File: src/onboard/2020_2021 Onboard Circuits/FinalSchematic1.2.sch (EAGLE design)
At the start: 79 parts, among them IC1 MIC2937A-5.0BT, IC3 A5975D

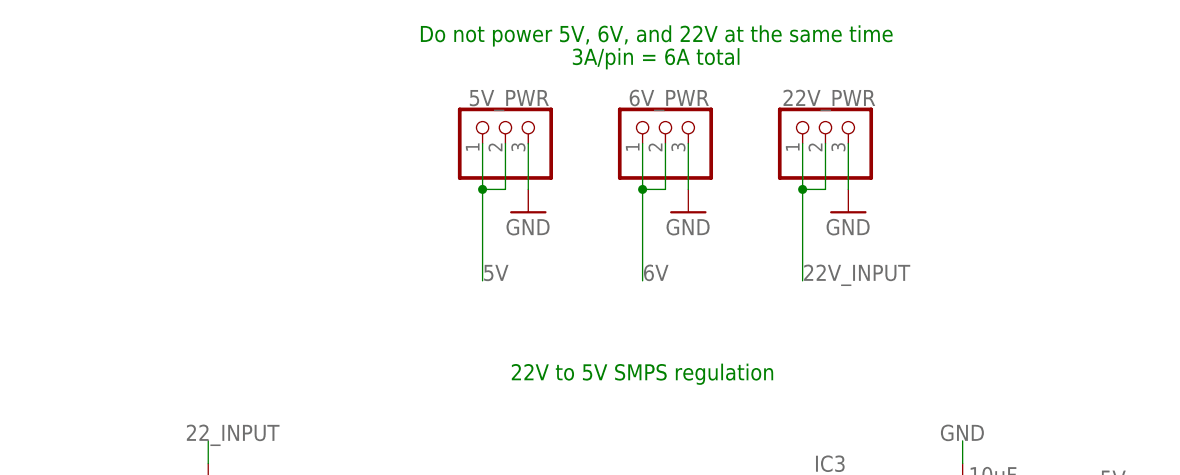
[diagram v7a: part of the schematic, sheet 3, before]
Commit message: Added bulk decoupling
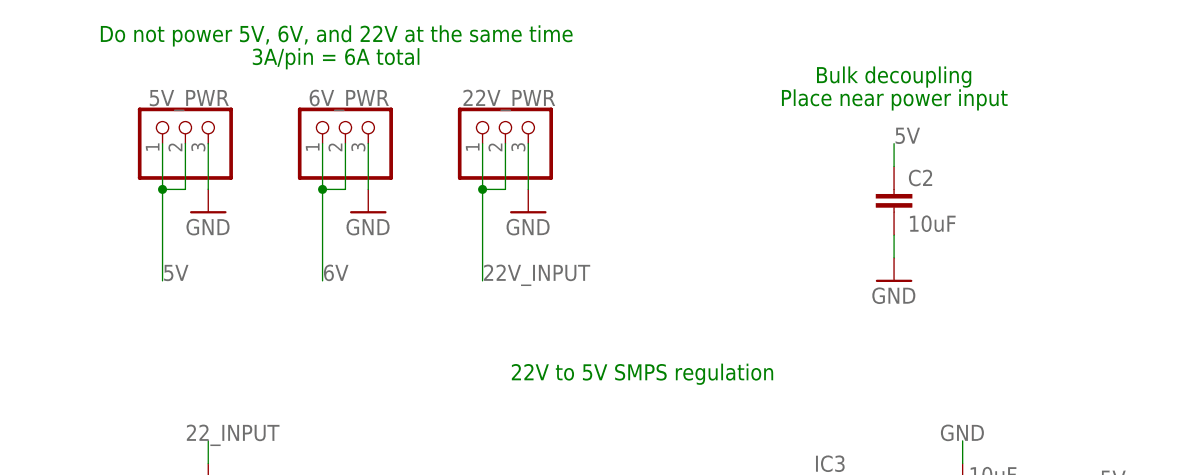
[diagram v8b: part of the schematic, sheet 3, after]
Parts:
- added C2: 10uF, capacitor-wima:C2,5-3
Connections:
- net 5V: now also C2.1
- net GND: now also C2.2
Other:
- note added: "Bulk decoupling"
- note added: "Place near power input"
- moved on the sheet: 22V_PWR, 5V_PWR, 6V_PWR
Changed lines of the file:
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@@
 <part name="GND12" library="supply1" library_urn="urn:adsk.eagle:library:371" deviceset="GND" device=""/>
 <part name="GND15" library="supply1" library_urn="urn:adsk.eagle:library:371" deviceset="GND" device=""/>
+<part name="C2" library="capacitor-wima" library_urn="urn:adsk.eagle:library:116" deviceset="C" device="2,5-3" package3d_urn="urn:adsk.eagle:package:5436/1" value="10uF"/>
+<part name="GND16" library="supply1" library_urn="urn:adsk.eagle:library:371" deviceset="GND" device=""/>
 </parts>
 <sheets>
@@
 <description>Voltage regulation</description>
 <plain>
-<text x="26.924" y="88.392" size="1.778" layer="91" align="center">Do not power 5V, 6V, and 22V at the same time</text>
-<text x="26.924" y="85.852" size="1.778" layer="91" align="center">3A/pin = 6A total</text>
+<text x="-8.636" y="88.392" size="1.778" layer="91" align="center">Do not power 5V, 6V, and 22V at the same time</text>
+<text x="-8.636" y="85.852" size="1.778" layer="91" align="center">3A/pin = 6A total</text>
 <text x="25.4" y="50.8" size="1.778" layer="91" align="center">22V to 5V SMPS regulation</text>
 <text x="22.86" y="-5.08" size="1.778" layer="91" align="center">6V to 5V LDO regulation</text>
+<text x="53.34" y="83.82" size="1.778" layer="91" align="center">Bulk decoupling</text>
+<text x="53.34" y="81.28" size="1.778" layer="91" align="center">Place near power input</text>
 </plain>
 <instances>
@@
 <attribute name="VALUE" x="67.056" y="40.259" size="1.778" layer="96" rot="R180"/>
 </instance>
-<instance part="GND11" gate="1" x="30.48" y="68.58" smashed="yes">
-<attribute name="VALUE" x="27.94" y="66.04" size="1.778" layer="96"/>
-</instance>
-<instance part="6V_PWR" gate="A" x="27.94" y="78.74" smashed="yes" rot="R90">
-<attribute name="NAME" x="28.321" y="81.28" size="1.778" layer="95" align="center"/>
-<attribute name="VALUE" x="35.56" y="72.39" size="1.778" layer="96" rot="R90"/>
-</instance>
-<instance part="22V_PWR" gate="A" x="45.72" y="78.74" smashed="yes" rot="R90">
-<attribute name="NAME" x="46.101" y="81.28" size="1.778" layer="95" align="center"/>
-<attribute name="VALUE" x="53.34" y="72.39" size="1.778" layer="96" rot="R90"/>
-</instance>
-<instance part="GND14" gate="1" x="48.26" y="68.58" smashed="yes">
-<attribute name="VALUE" x="45.72" y="66.04" size="1.778" layer="96"/>
+<instance part="GND11" gate="1" x="-5.08" y="68.58" smashed="yes">
+<attribute name="VALUE" x="-7.62" y="66.04" size="1.778" layer="96"/>
+</instance>
+<instance part="6V_PWR" gate="A" x="-7.62" y="78.74" smashed="yes" rot="R90">
+<attribute name="NAME" x="-7.239" y="81.28" size="1.778" layer="95" align="center"/>
+<attribute name="VALUE" x="0" y="72.39" size="1.778" layer="96" rot="R90"/>
+</instance>
+<instance part="22V_PWR" gate="A" x="10.16" y="78.74" smashed="yes" rot="R90">
+<attribute name="NAME" x="10.541" y="81.28" size="1.778" layer="95" align="center"/>
+<attribute name="VALUE" x="17.78" y="72.39" size="1.778" layer="96" rot="R90"/>
+</instance>
+<instance part="GND14" gate="1" x="12.7" y="68.58" smashed="yes">
+<attribute name="VALUE" x="10.16" y="66.04" size="1.778" layer="96"/>
 </instance>
 <instance part="R1" gate="G$1" x="-22.86" y="35.56" smashed="yes" rot="R90">
@@
 <attribute name="VALUE" x="-25.4" y="7.62" size="1.778" layer="96"/>
 </instance>
-<instance part="GND7" gate="1" x="12.7" y="68.58" smashed="yes">
-<attribute name="VALUE" x="10.16" y="66.04" size="1.778" layer="96"/>
-</instance>
-<instance part="5V_PWR" gate="A" x="10.16" y="78.74" smashed="yes" rot="R90">
-<attribute name="NAME" x="10.541" y="81.28" size="1.778" layer="95" align="center"/>
-<attribute name="VALUE" x="17.78" y="72.39" size="1.778" layer="96" rot="R90"/>
+<instance part="GND7" gate="1" x="-22.86" y="68.58" smashed="yes">
+<attribute name="VALUE" x="-25.4" y="66.04" size="1.778" layer="96"/>
+</instance>
+<instance part="5V_PWR" gate="A" x="-25.4" y="78.74" smashed="yes" rot="R90">
+<attribute name="NAME" x="-25.019" y="81.28" size="1.778" layer="95" align="center"/>
+<attribute name="VALUE" x="-17.78" y="72.39" size="1.778" layer="96" rot="R90"/>
 </instance>
 <instance part="IC1" gate="A1" x="20.32" y="-20.32" smashed="yes">
@@
 <attribute name="NAME" x="37.084" y="-22.479" size="1.778" layer="95"/>
 <attribute name="VALUE" x="37.084" y="-27.559" size="1.778" layer="96"/>
+</instance>
+<instance part="C2" gate="G$1" x="53.34" y="71.12" smashed="yes">
+<attribute name="NAME" x="54.864" y="71.501" size="1.778" layer="95"/>
+<attribute name="VALUE" x="54.864" y="66.421" size="1.778" layer="96"/>
+</instance>
+<instance part="GND16" gate="1" x="53.34" y="60.96" smashed="yes">
+<attribute name="VALUE" x="50.8" y="58.42" size="1.778" layer="96"/>
 </instance>
 </instances>
@@
 </segment>
 <segment>
-<wire x1="7.62" y1="76.2" x2="7.62" y2="71.12" width="0.1524" layer="91"/>
-<label x="7.62" y="60.96" size="1.778" layer="95"/>
+<wire x1="-27.94" y1="76.2" x2="-27.94" y2="71.12" width="0.1524" layer="91"/>
+<label x="-27.94" y="60.96" size="1.778" layer="95"/>
 <pinref part="5V_PWR" gate="A" pin="1"/>
 <pinref part="5V_PWR" gate="A" pin="2"/>
-<wire x1="7.62" y1="71.12" x2="7.62" y2="60.96" width="0.1524" layer="91"/>
-<wire x1="10.16" y1="76.2" x2="10.16" y2="71.12" width="0.1524" layer="91"/>
-<wire x1="10.16" y1="71.12" x2="7.62" y2="71.12" width="0.1524" layer="91"/>
-<junction x="7.62" y="71.12"/>
+<wire x1="-27.94" y1="71.12" x2="-27.94" y2="60.96" width="0.1524" layer="91"/>
+<wire x1="-25.4" y1="76.2" x2="-25.4" y2="71.12" width="0.1524" layer="91"/>
+<wire x1="-25.4" y1="71.12" x2="-27.94" y2="71.12" width="0.1524" layer="91"/>
+<junction x="-27.94" y="71.12"/>
 </segment>
 <segment>
@@
 <label x="48.26" y="-20.32" size="1.778" layer="95"/>
 </segment>
+<segment>
+<pinref part="C2" gate="G$1" pin="1"/>
+<wire x1="53.34" y1="73.66" x2="53.34" y2="76.2" width="0.1524" layer="91"/>
+<label x="53.34" y="76.2" size="1.778" layer="95"/>
+</segment>
 </net>
 <net name="3.3V" class="0">
@@
 </segment>
 <segment>
-<wire x1="30.48" y1="76.2" x2="30.48" y2="71.12" width="0.1524" layer="91"/>
+<wire x1="-5.08" y1="76.2" x2="-5.08" y2="71.12" width="0.1524" layer="91"/>
 <pinref part="GND11" gate="1" pin="GND"/>
 <pinref part="6V_PWR" gate="A" pin="3"/>
@@
 <segment>
 <pinref part="22V_PWR" gate="A" pin="3"/>
-<wire x1="48.26" y1="76.2" x2="48.26" y2="71.12" width="0.1524" layer="91"/>
+<wire x1="12.7" y1="76.2" x2="12.7" y2="71.12" width="0.1524" layer="91"/>
 <pinref part="GND14" gate="1" pin="GND"/>
 </segment>
@@
 </segment>
 <segment>
-<wire x1="12.7" y1="76.2" x2="12.7" y2="71.12" width="0.1524" layer="91"/>
+<wire x1="-22.86" y1="76.2" x2="-22.86" y2="71.12" width="0.1524" layer="91"/>
 <pinref part="GND7" gate="1" pin="GND"/>
 <pinref part="5V_PWR" gate="A" pin="3"/>
@@
 <wire x1="20.32" y1="-27.94" x2="20.32" y2="-30.48" width="0.1524" layer="91"/>
 <pinref part="GND8" gate="1" pin="GND"/>
+</segment>
+<segment>
+<pinref part="C2" gate="G$1" pin="2"/>
+<wire x1="53.34" y1="66.04" x2="53.34" y2="63.5" width="0.1524" layer="91"/>
+<pinref part="GND16" gate="1" pin="GND"/>
 </segment>
 </net>
@@
 <segment>
 <pinref part="22V_PWR" gate="A" pin="2"/>
-<wire x1="45.72" y1="76.2" x2="45.72" y2="71.12" width="0.1524" layer="91"/>
-<wire x1="45.72" y1="71.12" x2="43.18" y2="71.12" width="0.1524" layer="91"/>
+<wire x1="10.16" y1="76.2" x2="10.16" y2="71.12" width="0.1524" layer="91"/>
+<wire x1="10.16" y1="71.12" x2="7.62" y2="71.12" width="0.1524" layer="91"/>
 <pinref part="22V_PWR" gate="A" pin="1"/>
-<wire x1="43.18" y1="71.12" x2="43.18" y2="76.2" width="0.1524" layer="91"/>
-<wire x1="43.18" y1="60.96" x2="43.18" y2="71.12" width="0.1524" layer="91"/>
-<junction x="43.18" y="71.12"/>
-<label x="43.18" y="60.96" size="1.778" layer="95"/>
+<wire x1="7.62" y1="71.12" x2="7.62" y2="76.2" width="0.1524" layer="91"/>
+<wire x1="7.62" y1="60.96" x2="7.62" y2="71.12" width="0.1524" layer="91"/>
+<junction x="7.62" y="71.12"/>
+<label x="7.62" y="60.96" size="1.778" layer="95"/>
 </segment>
 </net>
@@
 <net name="6V" class="0">
 <segment>
-<wire x1="25.4" y1="76.2" x2="25.4" y2="71.12" width="0.1524" layer="91"/>
-<label x="25.4" y="60.96" size="1.778" layer="95"/>
+<wire x1="-10.16" y1="76.2" x2="-10.16" y2="71.12" width="0.1524" layer="91"/>
+<label x="-10.16" y="60.96" size="1.778" layer="95"/>
 <pinref part="6V_PWR" gate="A" pin="1"/>
 <pinref part="6V_PWR" gate="A" pin="2"/>
-<wire x1="25.4" y1="71.12" x2="25.4" y2="60.96" width="0.1524" layer="91"/>
-<wire x1="27.94" y1="76.2" x2="27.94" y2="71.12" width="0.1524" layer="91"/>
-<wire x1="27.94" y1="71.12" x2="25.4" y2="71.12" width="0.1524" layer="91"/>
-<junction x="25.4" y="71.12"/>
-</segment>
-<segment>
+<wire x1="-10.16" y1="71.12" x2="-10.16" y2="60.96" width="0.1524" layer="91"/>
+<wire x1="-7.62" y1="76.2" x2="-7.62" y2="71.12" width="0.1524" layer="91"/>
+<wire x1="-7.62" y1="71.12" x2="-10.16" y2="71.12" width="0.1524" layer="91"/>
+<junction x="-10.16" y="71.12"/>
+</segment>
+<segment>
